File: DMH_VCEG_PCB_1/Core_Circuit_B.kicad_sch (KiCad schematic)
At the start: 110 parts, among them J24 Conn_01x06_PinHeader, J25 Conn_01x10_PinHeader, J26 Conn_01x10_PinHeader, Q17 BC558, Q18 BC558, Q19 BC548, Q20 BC548, Q21 BS170, Q22 BS170, Q23 BC548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

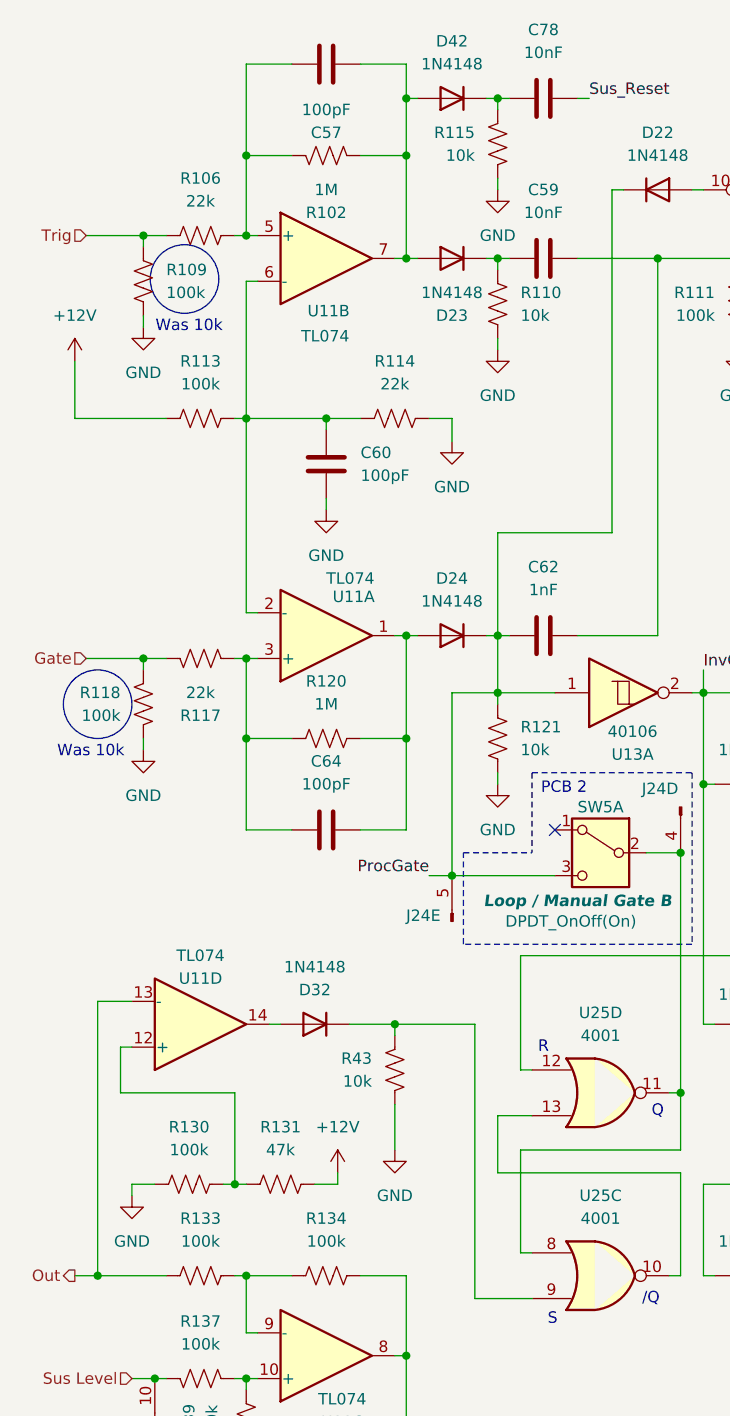
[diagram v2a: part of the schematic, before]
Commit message: Synced PCB 1 and 2
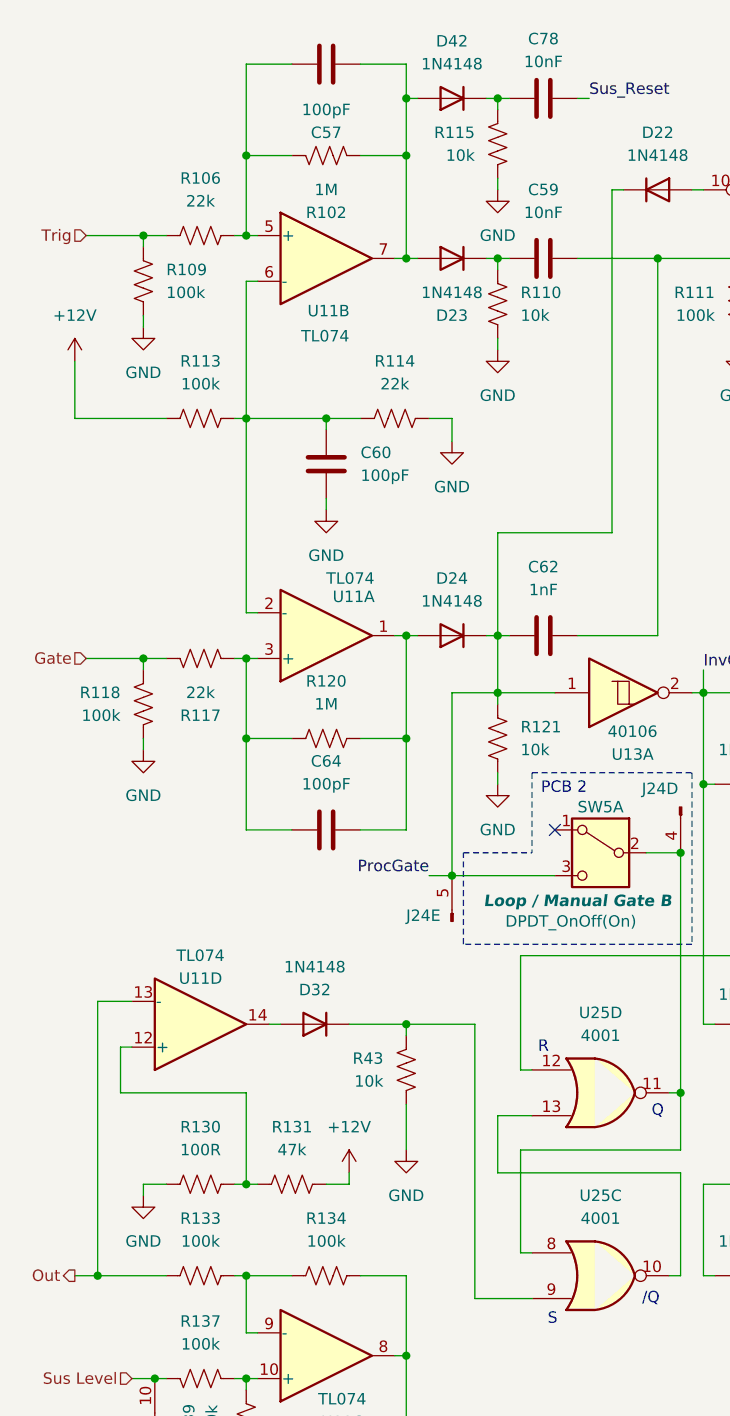
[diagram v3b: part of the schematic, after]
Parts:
- R130: value 100k -> 100R
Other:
- note removed: "Was 10k"
- moved on the sheet: R130, R131, R43
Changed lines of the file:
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@@
 		(comment 1 "PCB for 15cm Kosmo format synthesizer module")
 	)
-	(circle
-		(center 29.972 40.386)
-		(radius 3.81)
-		(stroke
-			(width 0)
-			(type default)
-		)
-		(fill
-			(type none)
-		)
-	)
 	(rectangle
 		(start 128.27 13.97)
@@
 		)
 	)
-	(circle
-		(center 20.32 87.63)
-		(radius 3.81)
-		(stroke
-			(width 0)
-			(type default)
-		)
-		(fill
-			(type none)
-		)
-	)
 	(text "PCB 2"
 		(exclude_from_sim no)
@@
 		)
 	)
-	(text "Was 10k"
-		(exclude_from_sim no)
-		(at 30.48 45.72 0)
-		(effects
-			(font
-				(size 1.27 1.27)
-			)
-		)
-	)
 	(text "R"
 		(exclude_from_sim no)
@@
 		)
 	)
-	(text "Was 10k"
-		(exclude_from_sim no)
-		(at 19.558 92.964 0)
-		(effects
-			(font
-				(size 1.27 1.27)
-			)
-		)
-	)
 	(junction
 		(at 125.73 96.52)
@@
 	)
 	(junction
-		(at 53.34 123.19)
-		(diameter 0)
-		(color 0 0 0 0)
-	)
-	(junction
 		(at 261.62 19.05)
 		(diameter 0)
@@
 	)
 	(junction
-		(at 35.56 140.97)
+		(at 36.83 140.97)
 		(diameter 0)
 		(color 0 0 0 0)
@@
 	)
 	(junction
+		(at 54.61 123.19)
+		(diameter 0)
+		(color 0 0 0 0)
+	)
+	(junction
 		(at 161.29 29.21)
 		(diameter 0)
@@
 	(wire
 		(pts
-			(xy 24.13 140.97) (xy 26.67 140.97)
+			(xy 25.4 140.97) (xy 27.94 140.97)
 		)
 		(stroke
@@
 	(wire
 		(pts
-			(xy 48.26 123.19) (xy 53.34 123.19)
+			(xy 48.26 123.19) (xy 54.61 123.19)
 		)
 		(stroke
@@
 	(wire
 		(pts
-			(xy 53.34 132.08) (xy 53.34 137.16)
+			(xy 54.61 132.08) (xy 54.61 137.16)
 		)
 		(stroke
@@
 	(wire
 		(pts
-			(xy 44.45 140.97) (xy 46.99 140.97)
+			(xy 45.72 140.97) (xy 48.26 140.97)
 		)
 		(stroke
@@
 	(wire
 		(pts
-			(xy 24.13 142.24) (xy 24.13 140.97)
+			(xy 25.4 142.24) (xy 25.4 140.97)
 		)
 		(stroke
@@
 	(wire
 		(pts
-			(xy 34.29 140.97) (xy 35.56 140.97)
+			(xy 35.56 140.97) (xy 36.83 140.97)
 		)
 		(stroke
@@
 	(wire
 		(pts
-			(xy 53.34 123.19) (xy 62.23 123.19)
-		)
-		(stroke
-			(width 0)
-			(type default)
-		)
-	)
-	(wire
-		(pts
 			(xy 113.03 52.07) (xy 114.3 52.07)
 		)
@@
 	(wire
 		(pts
-			(xy 35.56 130.81) (xy 35.56 140.97)
+			(xy 36.83 130.81) (xy 36.83 140.97)
 		)
 		(stroke
@@
 	(wire
 		(pts
-			(xy 22.86 130.81) (xy 35.56 130.81)
+			(xy 22.86 130.81) (xy 36.83 130.81)
 		)
 		(stroke
@@
 	(wire
 		(pts
-			(xy 35.56 140.97) (xy 36.83 140.97)
+			(xy 36.83 140.97) (xy 38.1 140.97)
 		)
 		(stroke
@@
 	(wire
 		(pts
-			(xy 53.34 123.19) (xy 53.34 124.46)
+			(xy 54.61 123.19) (xy 54.61 124.46)
 		)
 		(stroke
@@
 	(wire
 		(pts
+			(xy 54.61 123.19) (xy 62.23 123.19)
+		)
+		(stroke
+			(width 0)
+			(type default)
+		)
+	)
+	(wire
+		(pts
 			(xy 255.27 60.96) (xy 255.27 58.42)
 		)
@@
 	(wire
 		(pts
-			(xy 46.99 140.97) (xy 46.99 139.7)
+			(xy 48.26 140.97) (xy 48.26 139.7)
 		)
 		(stroke
@@
 	(symbol
 		(lib_id "power:GND")
-		(at 24.13 142.24 0)
+		(at 25.4 142.24 0)
 		(unit 1)
 		(exclude_from_sim no)
@@
 		(fields_autoplaced yes)
 		(property "Reference" "#PWR0124"
-			(at 24.13 148.59 0)
+			(at 25.4 148.59 0)
 			(effects
 				(font
@@
 		)
 		(property "Value" "GND"
-			(at 24.13 147.32 0)
+			(at 25.4 147.32 0)
 			(effects
 				(font
@@
 		)
 		(property "Footprint" ""
-			(at 24.13 142.24 0)
+			(at 25.4 142.24 0)
 			(effects
 				(font
@@
 		)
 		(property "Datasheet" ""
-			(at 24.13 142.24 0)
+			(at 25.4 142.24 0)
 			(effects
 				(font
@@
 		)
 		(property "Description" "Power symbol creates a global label with name \"GND\" , ground"
-			(at 24.13 142.24 0)
+			(at 25.4 142.24 0)
 			(effects
 				(font
@@
 	(symbol
 		(lib_id "Device:R_US")
-		(at 53.34 128.27 0)
+		(at 54.61 128.27 0)
 		(mirror x)
 		(unit 1)
@@
 		(dnp no)
 		(property "Reference" "R43"
-			(at 50.8 126.9999 0)
+			(at 52.07 126.9999 0)
 			(effects
 				(font
@@
 		)
 		(property "Value" "10k"
-			(at 50.8 129.5399 0)
+			(at 52.07 129.5399 0)
 			(effects
 				(font
@@
 		)
 		(property "Footprint" "Resistor_THT:R_Axial_DIN0207_L6.3mm_D2.5mm_P7.62mm_Horizontal"
-			(at 54.356 128.016 90)
+			(at 55.626 128.016 90)
 			(effects
 				(font
@@
 		)
 		(property "Datasheet" "~"
-			(at 53.34 128.27 0)
+			(at 54.61 128.27 0)
 			(effects
 				(font
@@
 		)
 		(property "Description" "Resistor, US symbol"
-			(at 53.34 128.27 0)
+			(at 54.61 128.27 0)
 			(effects
 				(font
@@
 		(dnp no)
 		(property "Reference" "C78"
-			(at 69.85 12.7 90)
+			(at 69.85 13.716 90)
 			(effects
 				(font
@@
 		)
 		(property "Value" "10nF"
-			(at 69.85 15.24 90)
+			(at 69.85 16.256 90)
 			(effects
 				(font
@@
 	(symbol
 		(lib_id "power:+12V")
-		(at 46.99 139.7 0)
+		(at 48.26 139.7 0)
 		(unit 1)
 		(exclude_from_sim no)
@@
 		(fields_autoplaced yes)
 		(property "Reference" "#PWR0121"
-			(at 46.99 143.51 0)
+			(at 48.26 143.51 0)
 			(effects
 				(font
@@
 		)
 		(property "Value" "+12V"
-			(at 46.99 134.62 0)
+			(at 48.26 134.62 0)
 			(effects
 				(font
@@
 		)
 		(property "Footprint" ""
-			(at 46.99 139.7 0)
+			(at 48.26 139.7 0)
 			(effects
 				(font
@@
 		)
 		(property "Datasheet" ""
-			(at 46.99 139.7 0)
+			(at 48.26 139.7 0)
 			(effects
 				(font
@@
 		)
 		(property "Description" "Power symbol creates a global label with name \"+12V\""
-			(at 46.99 139.7 0)
+			(at 48.26 139.7 0)
 			(effects
 				(font
@@
 	(symbol
 		(lib_id "Device:R_US")
-		(at 30.48 140.97 270)
+		(at 31.75 140.97 270)
 		(unit 1)
 		(exclude_from_sim no)
@@
 		(dnp no)
 		(property "Reference" "R130"
-			(at 30.48 134.62 90)
+			(at 31.75 134.62 90)
 			(effects
 				(font
@@
 			)
 		)
-		(property "Value" "100k"
-			(at 30.48 137.16 90)
+		(property "Value" "100R"
+			(at 31.75 137.16 90)
 			(effects
 				(font
@@
 		)
 		(property "Footprint" "Resistor_THT:R_Axial_DIN0207_L6.3mm_D2.5mm_P7.62mm_Horizontal"
-			(at 30.226 141.986 90)
+			(at 31.496 141.986 90)
 			(effects
 				(font
@@
 		)
 		(property "Datasheet" "~"
-			(at 30.48 140.97 0)
+			(at 31.75 140.97 0)
 			(effects
 				(font
@@
 		)
 		(property "Description" "Resistor, US symbol"
-			(at 30.48 140.97 0)
+			(at 31.75 140.97 0)
 			(effects
 				(font
@@
 			)
 		)
+		(property "Function" ""
+			(at 31.75 140.97 0)
+			(effects
+				(font
+					(size 1.27 1.27)
+				)
+			)
+		)
 		(pin "2"
 		)
@@
 	(symbol
 		(lib_id "Device:R_US")
-		(at 40.64 140.97 270)
+		(at 41.91 140.97 270)
 		(unit 1)
 		(exclude_from_sim no)
@@
 		(dnp no)
 		(property "Reference" "R131"
-			(at 40.64 134.62 90)
+			(at 41.91 134.62 90)
 			(effects
 				(font
@@
 		)
 		(property "Value" "47k"
-			(at 40.64 137.16 90)
+			(at 41.91 137.16 90)
 			(effects
 				(font
@@
 		)
 		(property "Footprint" "Resistor_THT:R_Axial_DIN0207_L6.3mm_D2.5mm_P7.62mm_Horizontal"
-			(at 40.386 141.986 90)
+			(at 41.656 141.986 90)
 			(effects
 				(font
@@
 		)
 		(property "Datasheet" "~"
-			(at 40.64 140.97 0)
+			(at 41.91 140.97 0)
 			(effects
 				(font
@@
 		)
 		(property "Description" "Resistor, US symbol"
-			(at 40.64 140.97 0)
+			(at 41.91 140.97 0)
 			(effects
 				(font
@@
 	(symbol
 		(lib_id "power:GND")
-		(at 53.34 137.16 0)
+		(at 54.61 137.16 0)
 		(unit 1)
 		(exclude_from_sim no)
@@
 		(fields_autoplaced yes)
 		(property "Reference" "#PWR0131"
-			(at 53.34 143.51 0)
+			(at 54.61 143.51 0)
 			(effects
 				(font
@@
 		)
 		(property "Value" "GND"
-			(at 53.34 142.24 0)
+			(at 54.61 142.24 0)
 			(effects
 				(font
@@
 		)
 		(property "Footprint" ""
-			(at 53.34 137.16 0)
+			(at 54.61 137.16 0)
 			(effects
 				(font
@@
 		)
 		(property "Datasheet" ""
-			(at 53.34 137.16 0)
+			(at 54.61 137.16 0)
 			(effects
 				(font
@@
 		)
 		(property "Description" "Power symbol creates a global label with name \"GND\" , ground"
-			(at 53.34 137.16 0)
+			(at 54.61 137.16 0)
 			(effects
 				(font

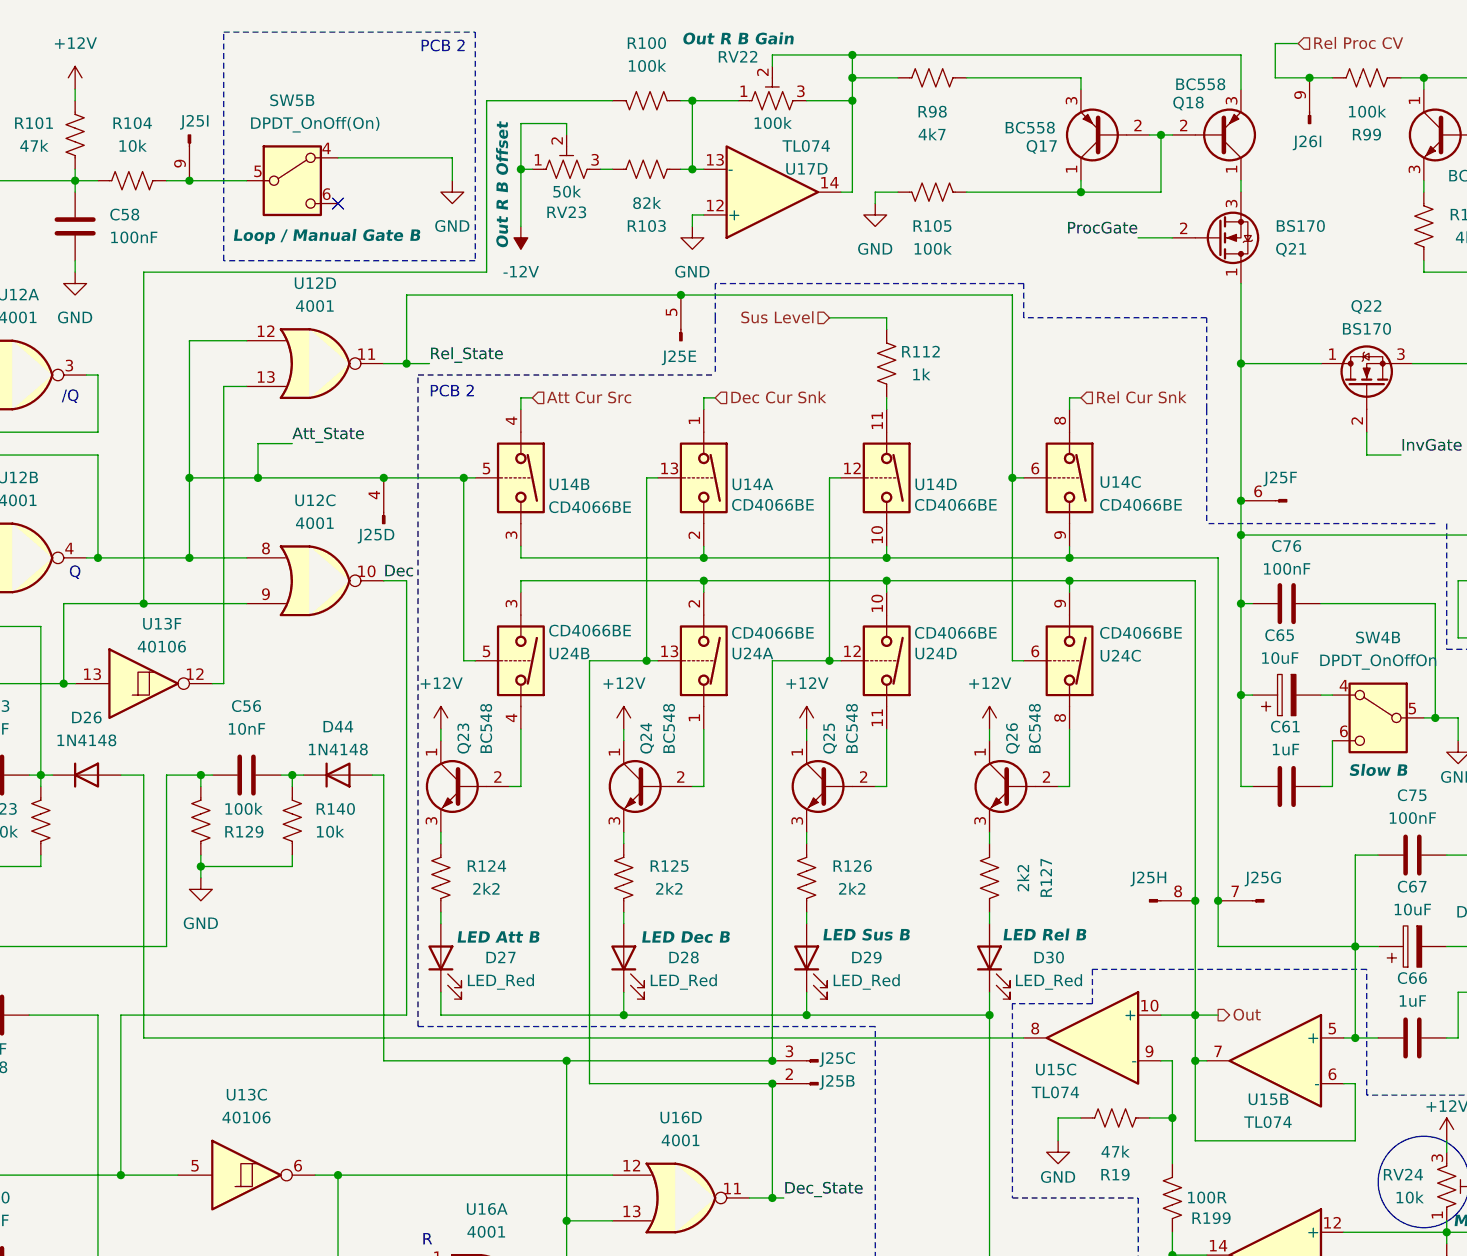
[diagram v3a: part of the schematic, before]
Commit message: Synced PCB 2 schematic to PCB 1
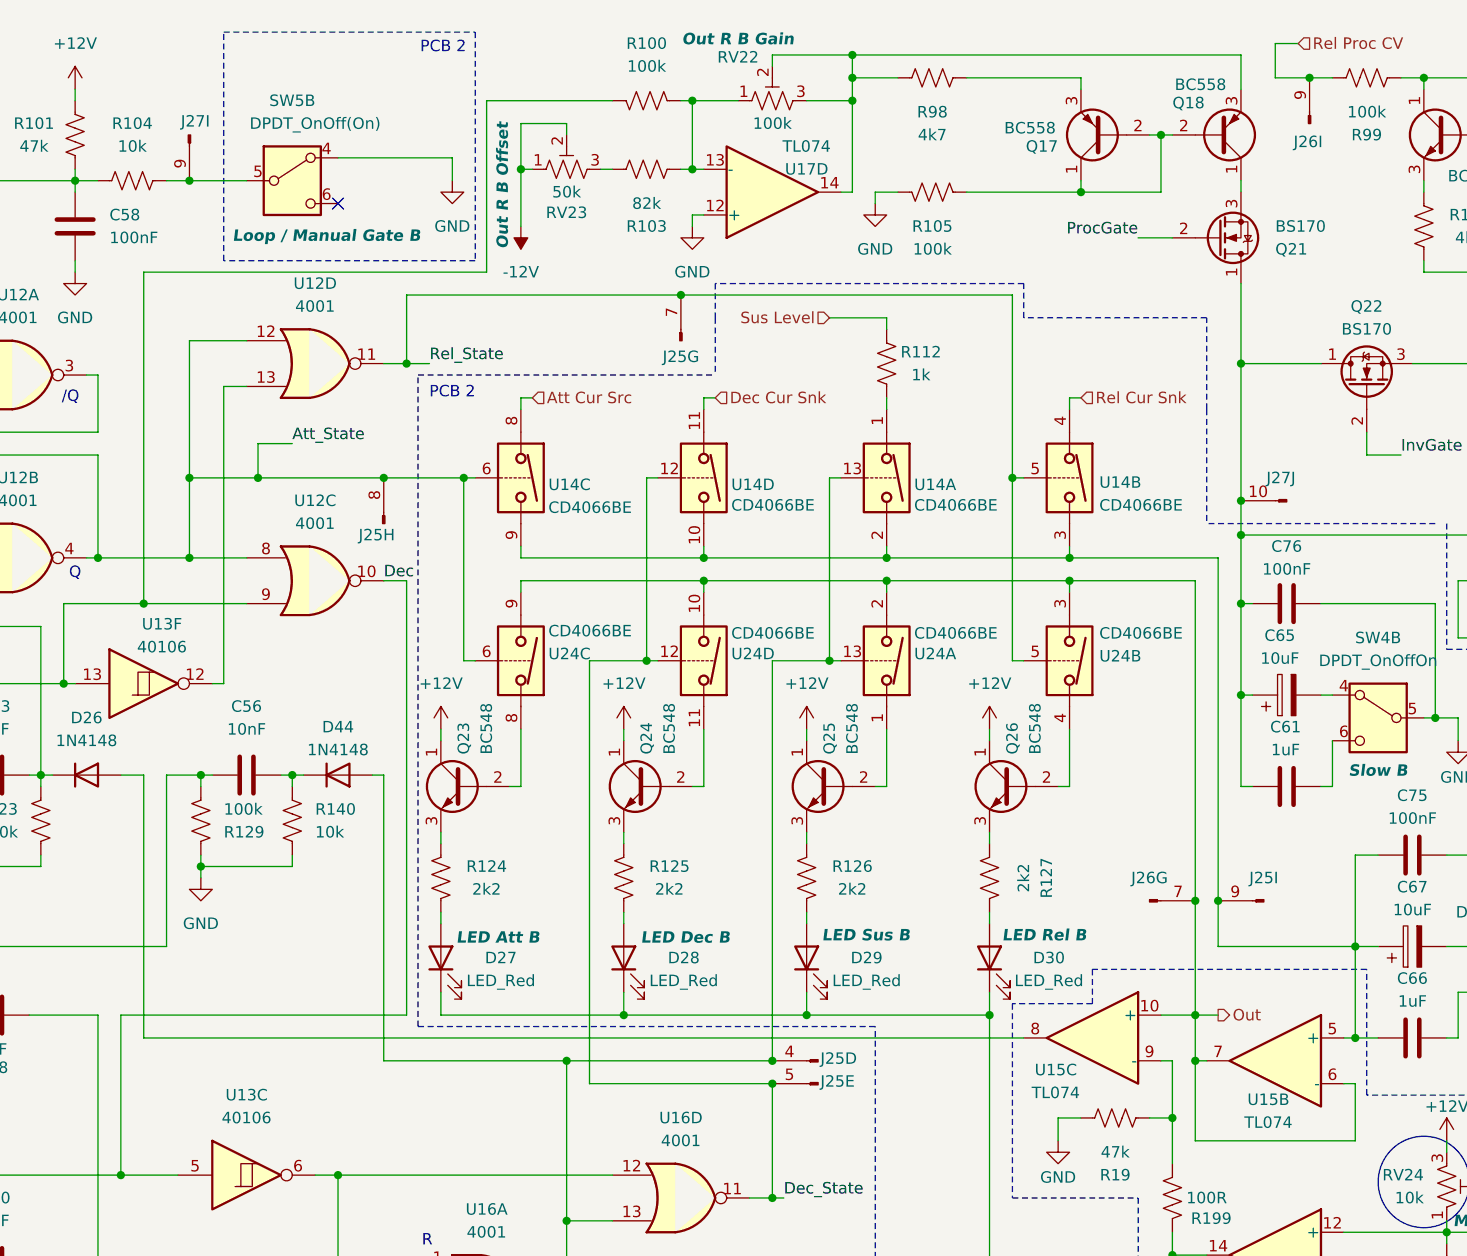
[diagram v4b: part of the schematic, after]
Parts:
- renumbered J25 to J26, J25 to J27
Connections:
- net Att Cur Src: now also U14.8; no longer U14.4
- net Att_State: now also J25.8 (Pin_8), U14.6, U24.6; no longer J25.4 (Pin_4), U14.5, U24.5
- net Dec Cur Snk: now also U14.11; no longer U14.1
- net Dec_State: now also J25.5 (Pin_5), U14.12, U24.12; no longer J25.2 (Pin_2), U14.13, U24.13
- net Out: now also J26.7 (Pin_7), U24.10, U24.2, U24.3, U24.9; no longer J26.8 (Pin_8), U24.10, U24.2, U24.3, U24.9
- net Rel Cur Snk: now also U14.4; no longer U14.8
- net Rel_State: now also J25.7 (Pin_7), U14.5, U24.5; no longer J25.5 (Pin_5), U14.6, U24.6
- net Sus_State: now also J25.4 (Pin_4), U14.13, U24.13; no longer J25.3 (Pin_3), U14.12, U24.12
- net at Q23.2 (B): now also U24.8; no longer U24.4
- net at C61.2, C65.1, C76.2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: now also J27.10 (Pin_10); no longer J27.6 (Pin_6)
- net at Q25.2 (B): now also U24.1; no longer U24.11
- net at Q26.2 (B): now also U24.4; no longer U24.8
- net at R112.1: now also U14.1; no longer U14.11
- net at Q24.2 (B): now also U24.11; no longer U24.1
- new net: C66.1, C67.1, C75.2, J25.9 (Pin_9), U14.10, U14.2, U14.3, U14.9, U15.5 (+)
